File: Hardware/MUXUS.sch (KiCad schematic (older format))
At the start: 119 parts, among them J1 USB_C_Receptacle_USB2.0, J2 USB_B, J3 USB_A, J4 USB_B, J5 USB_A, J6 STDC14, J7 USB_B, J8 USB_A, SW1 USER, SW2 RESET, U1 USBLC6-4SC6, U10 AP2151W, U11 AOZ1212AI, U12 USBLC6-2SC6, U13 USBLC6-2SC6, U14 AP2151W, U2 USB2504A-JT, U3 USBLC6-2SC6, U4 USBLC6-2SC6, U5 AP2151W, U6 TS3USBCA420RSVR, U7 STM32G431K8T6, U8 USBLC6-2SC6, U9 USBLC6-2SC6, Y1 ATS240C

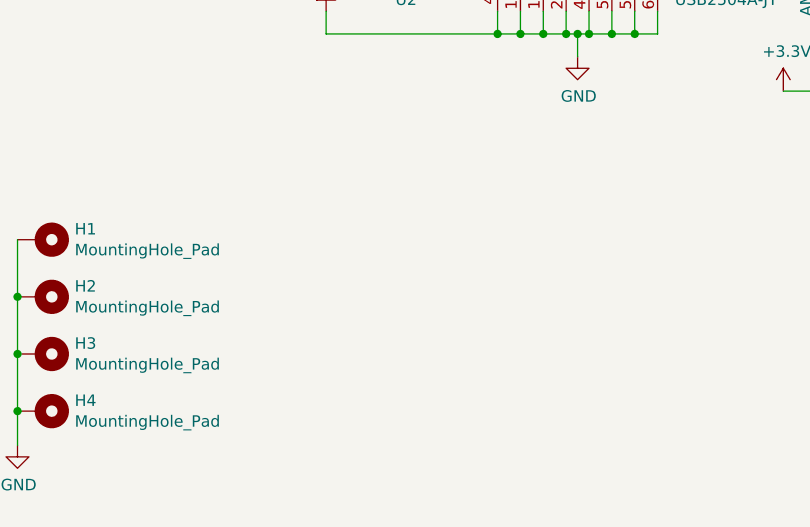
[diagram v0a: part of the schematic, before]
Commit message: AMOGUS and USB C footprint update
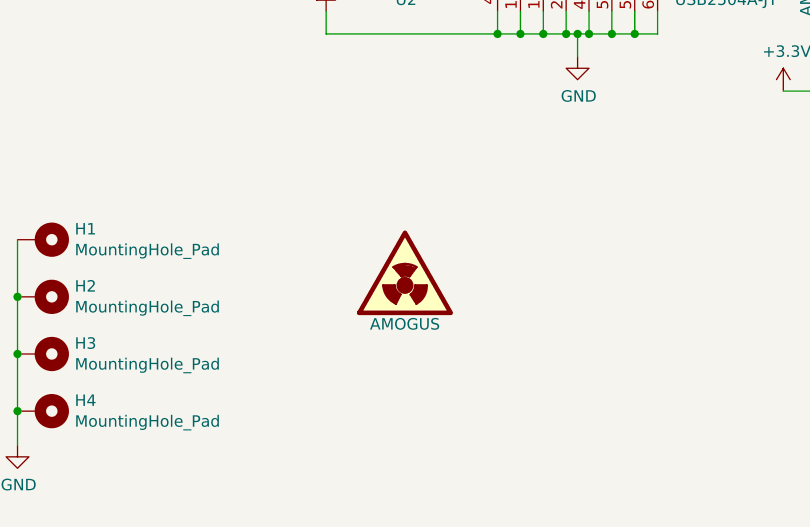
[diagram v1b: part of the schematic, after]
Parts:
- added SYM1: AMOGUS, AMOGUS:SUS, symbol Graphic:SYM_Radioactive_Large
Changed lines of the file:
@@
 Wire Wire Line
 	2150 1650 3250 1650
+$Comp
+L Graphic:SYM_Radioactive_Large SYM1
+U 1 1 615445FF
+P 2450 10200
+F 0 "SYM1" H 2545 10480 50  0001 C CNN
+F 1 "AMOGUS" H 2545 10030 50  0000 C CNN
+F 2 "AMOGUS:SUS" H 2545 10080 50  0001 C CNN
+F 3 "~" H 2575 10080 50  0001 C CNN
+	1    2450 10200
+	1    0    0    -1
+$EndComp
 $EndSCHEMATC

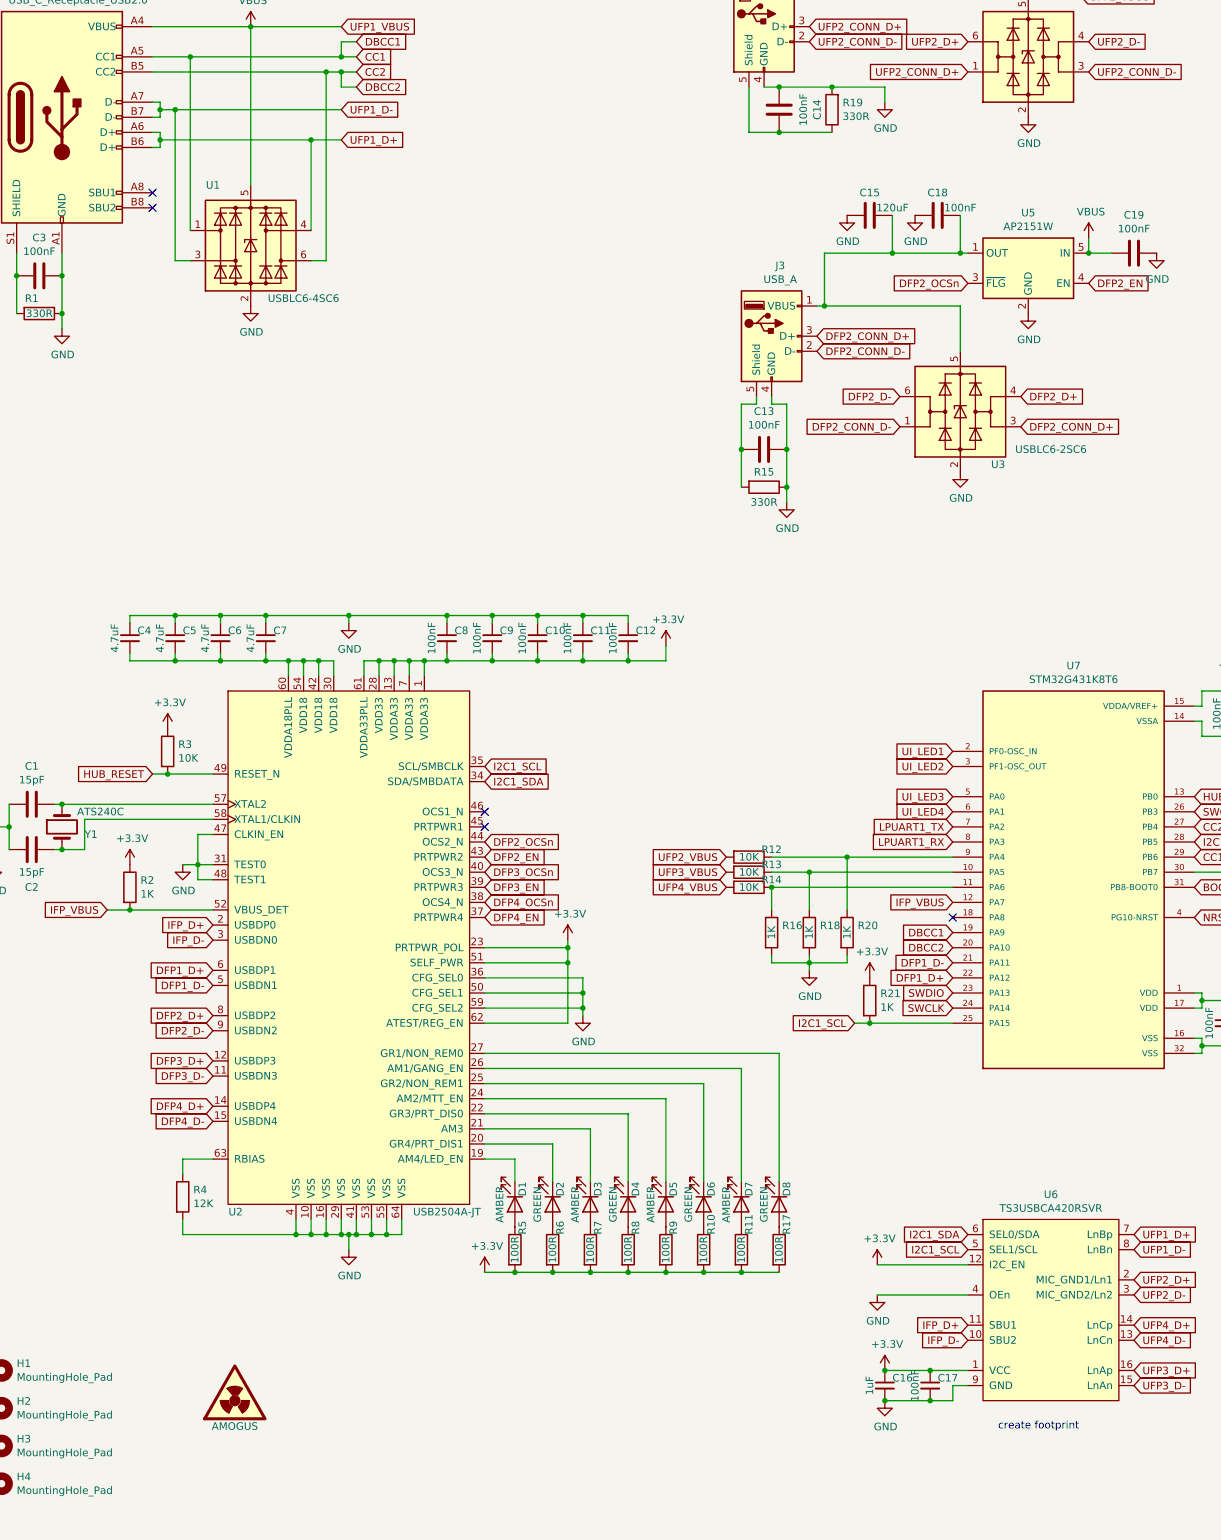
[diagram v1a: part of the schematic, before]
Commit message: First PCB routing
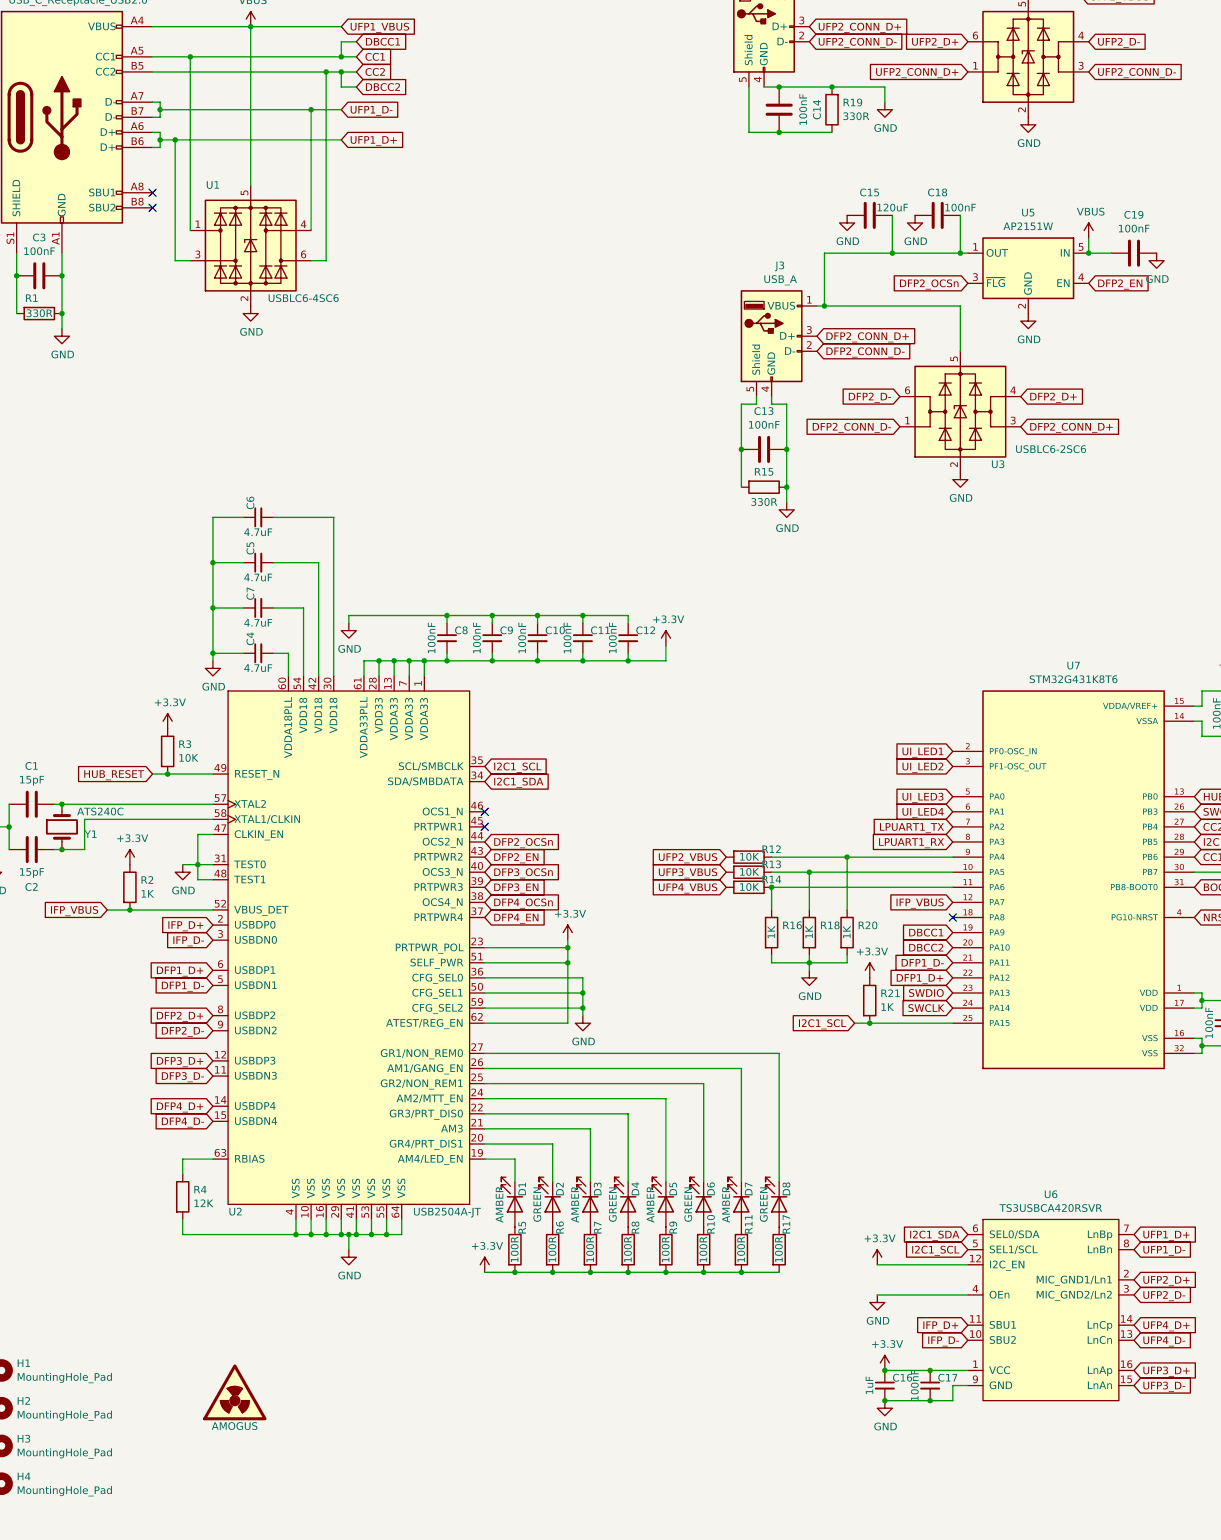
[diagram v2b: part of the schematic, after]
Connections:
- net UFP1_D+: now also U1.3 (I/O2); no longer U1.4 (I/O3)
- net UFP1_D-: now also U1.4 (I/O3); no longer U1.3 (I/O2)
- new net: C6.2, U2.30 (VDD18)
- new net: C5.2, U2.42 (VDD18)
- new net: C7.2, U2.54 (VDD18)
- new net: C4.2, U2.60 (VDDA18PLL)
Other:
- note removed: "create footprint"
- moved on the sheet: C4, C5, C6, C7
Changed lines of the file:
@@
 Wire Wire Line
 	10850 2600 10400 2600
-$Comp
-L Power_Protection:USBLC6-4SC6 U1
-U 1 1 61A4E349
-P 2650 2550
-F 0 "U1" H 2400 2950 50  0000 C CNN
-F 1 "USBLC6-4SC6" H 3000 2200 50  0000 C CNN
-F 2 "Package_TO_SOT_SMD:SOT-23-6" H 2650 2050 50  0001 C CNN
-F 3 "https://www.st.com/resource/en/datasheet/usblc6-4.pdf" H 2850 2900 50  0001 C CNN
-	1    2650 2550
-	1    0    0    -1
-$EndComp
 Wire Wire Line
 	2250 2650 2150 2650
@@
 Connection ~ 3700 5300
 Wire Wire Line
-	3200 5400 3200 5300
-Wire Wire Line
-	3200 5300 3100 5300
-Wire Wire Line
-	3100 5300 3100 5400
-Wire Wire Line
-	3100 5300 3000 5300
-Wire Wire Line
-	3000 5300 3000 5400
-Connection ~ 3100 5300
-Wire Wire Line
-	3000 5300 2900 5300
-Wire Wire Line
-	2900 5300 2900 5400
-Connection ~ 3000 5300
-Wire Wire Line
 	2950 9000 2950 9100
 Wire Wire Line
@@
 L Device:C_Small C7
 U 1 1 61858442
-P 2750 5150
-F 0 "C7" H 2800 5200 50  0000 L CNN
-F 1 "4.7uF" V 2650 5150 50  0000 C CNN
-F 2 "Capacitor_SMD:C_1206_3216Metric" H 2750 5150 50  0001 C CNN
-F 3 "~" H 2750 5150 50  0001 C CNN
-	1    2750 5150
-	1    0    0    -1
+P 2700 4950
+F 0 "C7" H 2750 5000 50  0000 L CNN
+F 1 "4.7uF" V 2600 4950 50  0000 C CNN
+F 2 "Capacitor_SMD:C_1206_3216Metric" H 2700 4950 50  0001 C CNN
+F 3 "~" H 2700 4950 50  0001 C CNN
+	1    2700 4950
+	0    -1   -1   0
 $EndComp
 $Comp
 L Device:C_Small C6
 U 1 1 6185AB3C
-P 2450 5150
-F 0 "C6" H 2500 5200 50  0000 L CNN
-F 1 "4.7uF" V 2350 5150 50  0000 C CNN
-F 2 "Capacitor_SMD:C_1206_3216Metric" H 2450 5150 50  0001 C CNN
-F 3 "~" H 2450 5150 50  0001 C CNN
-	1    2450 5150
-	1    0    0    -1
+P 2700 4350
+F 0 "C6" H 2750 4400 50  0000 L CNN
+F 1 "4.7uF" V 2600 4350 50  0000 C CNN
+F 2 "Capacitor_SMD:C_1206_3216Metric" H 2700 4350 50  0001 C CNN
+F 3 "~" H 2700 4350 50  0001 C CNN
+	1    2700 4350
+	0    -1   -1   0
 $EndComp
 $Comp
 L Device:C_Small C5
 U 1 1 6185B25D
-P 2150 5150
-F 0 "C5" H 2200 5200 50  0000 L CNN
-F 1 "4.7uF" V 2050 5150 50  0000 C CNN
-F 2 "Capacitor_SMD:C_1206_3216Metric" H 2150 5150 50  0001 C CNN
-F 3 "~" H 2150 5150 50  0001 C CNN
-	1    2150 5150
-	1    0    0    -1
+P 2700 4650
+F 0 "C5" H 2750 4700 50  0000 L CNN
+F 1 "4.7uF" V 2600 4650 50  0000 C CNN
+F 2 "Capacitor_SMD:C_1206_3216Metric" H 2700 4650 50  0001 C CNN
+F 3 "~" H 2700 4650 50  0001 C CNN
+	1    2700 4650
+	0    -1   -1   0
 $EndComp
 $Comp
 L Device:C_Small C4
 U 1 1 6185BAAA
-P 1850 5150
-F 0 "C4" H 1900 5200 50  0000 L CNN
-F 1 "4.7uF" V 1750 5150 50  0000 C CNN
-F 2 "Capacitor_SMD:C_1206_3216Metric" H 1850 5150 50  0001 C CNN
-F 3 "~" H 1850 5150 50  0001 C CNN
-	1    1850 5150
-	1    0    0    -1
+P 2700 5250
+F 0 "C4" H 2750 5300 50  0000 L CNN
+F 1 "4.7uF" V 2600 5250 50  0000 C CNN
+F 2 "Capacitor_SMD:C_1206_3216Metric" H 2700 5250 50  0001 C CNN
+F 3 "~" H 2700 5250 50  0001 C CNN
+	1    2700 5250
+	0    -1   -1   0
 $EndComp
 $Comp
@@
 	3950 5300 4250 5300
 Wire Wire Line
-	2750 5250 2750 5300
-Wire Wire Line
-	2750 5300 2900 5300
-Connection ~ 2900 5300
-Wire Wire Line
-	2450 5250 2450 5300
-Wire Wire Line
-	2450 5300 2750 5300
-Connection ~ 2750 5300
-Wire Wire Line
-	2150 5250 2150 5300
-Wire Wire Line
-	2150 5300 2450 5300
-Connection ~ 2450 5300
-Wire Wire Line
-	1850 5250 1850 5300
-Wire Wire Line
-	1850 5300 2150 5300
-Connection ~ 2150 5300
-Wire Wire Line
 	3950 5050 3950 5000
 Wire Wire Line
@@
 Wire Wire Line
 	4550 5000 4850 5000
-Wire Wire Line
-	1850 5050 1850 5000
-Wire Wire Line
-	1850 5000 2150 5000
-Wire Wire Line
-	2750 5000 2750 5050
-Wire Wire Line
-	2450 5050 2450 5000
-Connection ~ 2450 5000
-Wire Wire Line
-	2450 5000 2750 5000
-Wire Wire Line
-	2150 5050 2150 5000
-Connection ~ 2150 5000
-Wire Wire Line
-	2150 5000 2450 5000
 $Comp
 L power:GND #PWR08
@@
 	3300 5050 3300 5000
 Wire Wire Line
-	3300 5000 2750 5000
-Connection ~ 2750 5000
-Wire Wire Line
 	3300 5000 3950 5000
-Connection ~ 3300 5000
 Connection ~ 3950 5000
 $Comp
@@
 	15150 900  14800 900
 Connection ~ 14800 900
-Text Notes 7600 10400 0    50   ~ 0
-create footprint
 Connection ~ 12900 3900
 Wire Wire Line
@@
 $EndComp
 Wire Wire Line
-	2050 1850 3050 1850
-Wire Wire Line
-	2050 1650 2150 1650
-Wire Wire Line
 	2000 1300 2250 1300
 Wire Wire Line
@@
 Wire Wire Line
 	2250 1300 3250 1300
-Wire Wire Line
-	3050 1850 3050 2450
-Connection ~ 3050 1850
-Wire Wire Line
-	3050 1850 3250 1850
-Wire Wire Line
-	2150 2650 2150 1650
-Connection ~ 2150 1650
-Wire Wire Line
-	2150 1650 3250 1650
 $Comp
 L Graphic:SYM_Radioactive_Large SYM1
@@
 	1    0    0    -1
 $EndComp
+$Comp
+L Power_Protection:USBLC6-4SC6 U1
+U 1 1 61A4E349
+P 2650 2550
+F 0 "U1" H 2400 2950 50  0000 C CNN
+F 1 "USBLC6-4SC6" H 3000 2200 50  0000 C CNN
+F 2 "Package_TO_SOT_SMD:SOT-23-6" H 2650 2050 50  0001 C CNN
+F 3 "https://www.st.com/resource/en/datasheet/usblc6-4.pdf" H 2850 2900 50  0001 C CNN
+	1    2650 2550
+	1    0    0    -1
+$EndComp
+Wire Wire Line
+	2050 1850 2150 1850
+Wire Wire Line
+	2150 2650 2150 1850
+Connection ~ 2150 1850
+Wire Wire Line
+	2150 1850 3250 1850
+Wire Wire Line
+	3050 2450 3050 1650
+Wire Wire Line
+	2050 1650 3050 1650
+Connection ~ 3050 1650
+Wire Wire Line
+	3050 1650 3250 1650
+Wire Wire Line
+	3000 4950 3000 5400
+Wire Wire Line
+	2800 4950 3000 4950
+Wire Wire Line
+	3200 4350 3200 5400
+Wire Wire Line
+	2800 4350 3200 4350
+Wire Wire Line
+	3100 4650 3100 5400
+Wire Wire Line
+	2800 4650 3100 4650
+Wire Wire Line
+	2900 5250 2900 5400
+Wire Wire Line
+	2800 5250 2900 5250
+$Comp
+L power:GND #PWR0101
+U 1 1 619EDDCA
+P 2400 5300
+F 0 "#PWR0101" H 2400 5050 50  0001 C CNN
+F 1 "GND" H 2405 5127 50  0000 C CNN
+F 2 "" H 2400 5300 50  0001 C CNN
+F 3 "" H 2400 5300 50  0001 C CNN
+	1    2400 5300
+	1    0    0    -1
+$EndComp
+Wire Wire Line
+	2400 5300 2400 5250
+Wire Wire Line
+	2400 5250 2600 5250
+Wire Wire Line
+	2400 4950 2400 5250
+Wire Wire Line
+	2400 4950 2600 4950
+Connection ~ 2400 5250
+Wire Wire Line
+	2400 4650 2400 4950
+Wire Wire Line
+	2400 4650 2600 4650
+Connection ~ 2400 4950
+Wire Wire Line
+	2400 4350 2400 4650
+Wire Wire Line
+	2400 4350 2600 4350
+Connection ~ 2400 4650
 $EndSCHEMATC

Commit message: DEBUG connectors and VIAS
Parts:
- added J10: VCP, Connector_PinHeader_2.54mm:PinHeader_1x02_P2.54mm_Vertical, symbol Connector_Generic:Conn_01x02
- added J9: SWD, Connector_PinHeader_2.54mm:PinHeader_1x06_P2.54mm_Vertical, symbol Connector_Generic:Conn_01x06
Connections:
- net +3V3: now also J9.1 (Pin_1)
- net GND: now also J9.3 (Pin_3)
- net LPUART1_RX: now also J10.2 (Pin_2)
- net LPUART1_TX: now also J10.1 (Pin_1)
- net NRST: now also J9.5 (Pin_5)
- net SWCLK: now also J9.2 (Pin_2)
- net SWDIO: now also J9.4 (Pin_4)
- net SWO: now also J9.6 (Pin_6)
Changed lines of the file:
@@
 	2400 4350 2600 4350
 Connection ~ 2400 4650
+$Comp
+L Connector_Generic:Conn_01x06 J9
+U 1 1 615B40A3
+P 12450 8450
+F 0 "J9" H 12530 8442 50  0000 L CNN
+F 1 "SWD" H 12530 8351 50  0000 L CNN
+F 2 "Connector_PinHeader_2.54mm:PinHeader_1x06_P2.54mm_Vertical" H 12450 8450 50  0001 C CNN
+F 3 "~" H 12450 8450 50  0001 C CNN
+	1    12450 8450
+	1    0    0    -1
+$EndComp
+$Comp
+L Connector_Generic:Conn_01x02 J10
+U 1 1 615B75B8
+P 12450 8950
+F 0 "J10" H 12530 8942 50  0000 L CNN
+F 1 "VCP" H 12530 8851 50  0000 L CNN
+F 2 "Connector_PinHeader_2.54mm:PinHeader_1x02_P2.54mm_Vertical" H 12450 8950 50  0001 C CNN
+F 3 "~" H 12450 8950 50  0001 C CNN
+	1    12450 8950
+	1    0    0    -1
+$EndComp
+$Comp
+L power:+3.3V #PWR063
+U 1 1 615B80D0
+P 11900 8250
+F 0 "#PWR063" H 11900 8100 50  0001 C CNN
+F 1 "+3.3V" H 11915 8423 50  0000 C CNN
+F 2 "" H 11900 8250 50  0001 C CNN
+F 3 "" H 11900 8250 50  0001 C CNN
+	1    11900 8250
+	1    0    0    -1
+$EndComp
+Wire Wire Line
+	11900 8250 12250 8250
+Text GLabel 12250 8350 0    50   Input ~ 0
+SWCLK
+$Comp
+L power:GND #PWR064
+U 1 1 615DED53
+P 11900 8450
+F 0 "#PWR064" H 11900 8200 50  0001 C CNN
+F 1 "GND" H 11905 8277 50  0000 C CNN
+F 2 "" H 11900 8450 50  0001 C CNN
+F 3 "" H 11900 8450 50  0001 C CNN
+	1    11900 8450
+	1    0    0    -1
+$EndComp
+Wire Wire Line
+	11900 8450 12250 8450
+Text GLabel 12250 8550 0    50   Input ~ 0
+SWDIO
+Text GLabel 12250 8650 0    50   Input ~ 0
+NRST
+Text GLabel 12250 8750 0    50   Input ~ 0
+SWO
+Text GLabel 12250 8950 0    50   Input ~ 0
+LPUART1_TX
+Text GLabel 12250 9050 0    50   Input ~ 0
+LPUART1_RX
 $EndSCHEMATC
